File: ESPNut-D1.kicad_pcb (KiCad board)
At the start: 2 copper layers, 44 x 20 mm, 95 parts, among them J1 USB_C_Receptacle_USB2.0, J2 USB_PADS, J3 ESP_CONN, J4 ESP_CONN, J5 ESP_PROG, Q1 MMBT3904T-7-F, Q2 MMBT3904T-7-F, Q3 MMBT3906T-7-F, Q4 MMBT3906T-7-F, SW1 ESP_RST, SW2 ESP_BOOT, SW3 ESP_VDD_SW, SW4 ESPV_SEL, SW5 POW_CTRL, U1 CH340G, U2 MIC5219-3.3YM5, U3 AP22804AW5, Y1 12MHz

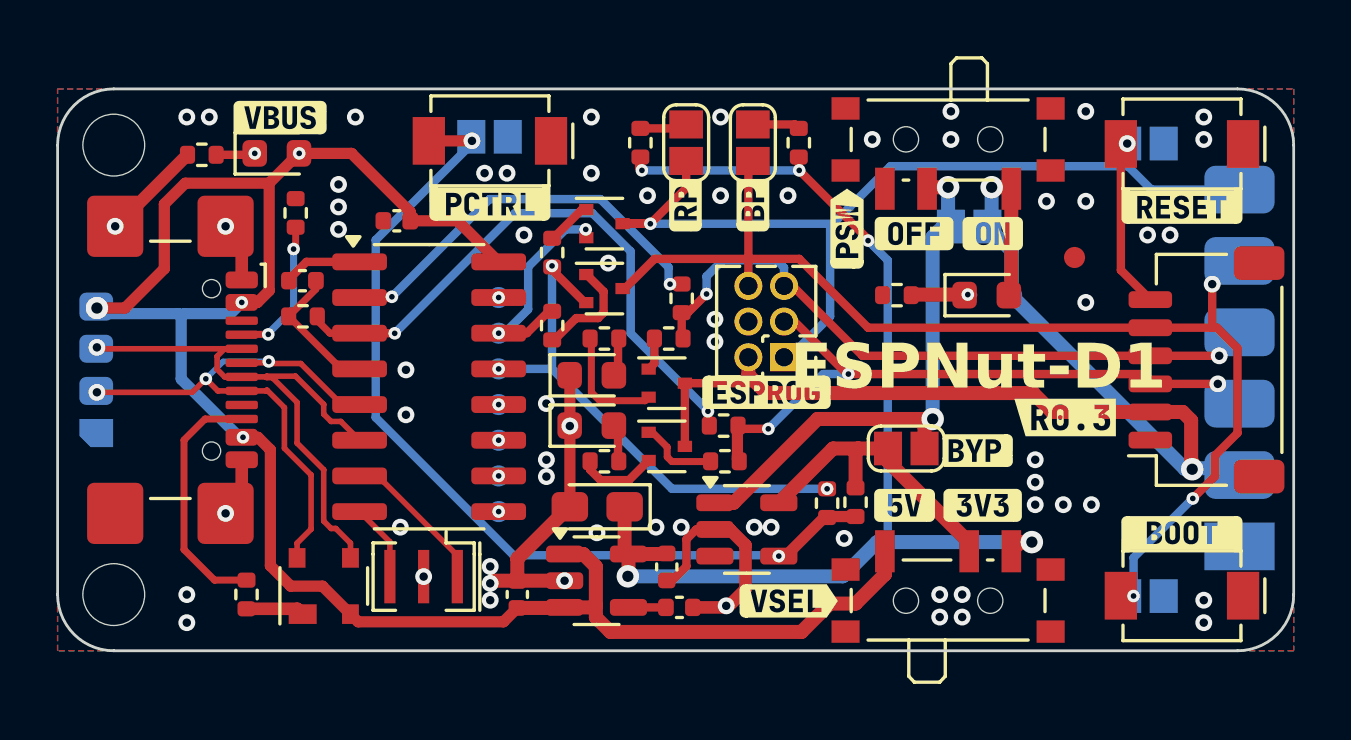
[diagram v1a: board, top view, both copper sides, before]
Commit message: Added `47 uF` 0805 capacitors
- Schematic
  - Added `47 uF` 0805 capacitors to the VBUS line, near the CH340 and `ESP_VDD_I`.
    - This was required because it was observed that the CH340 will reset when a significant load is connected to the `VBUS` line.
    - Adding two 22 uF capacitors proved to solve the issue.
    - But we are going to use 47 uF capacitors for better stability.
- PCB
  - Imported all changes to the PCB.
  - DRC passes.
- No version changes.
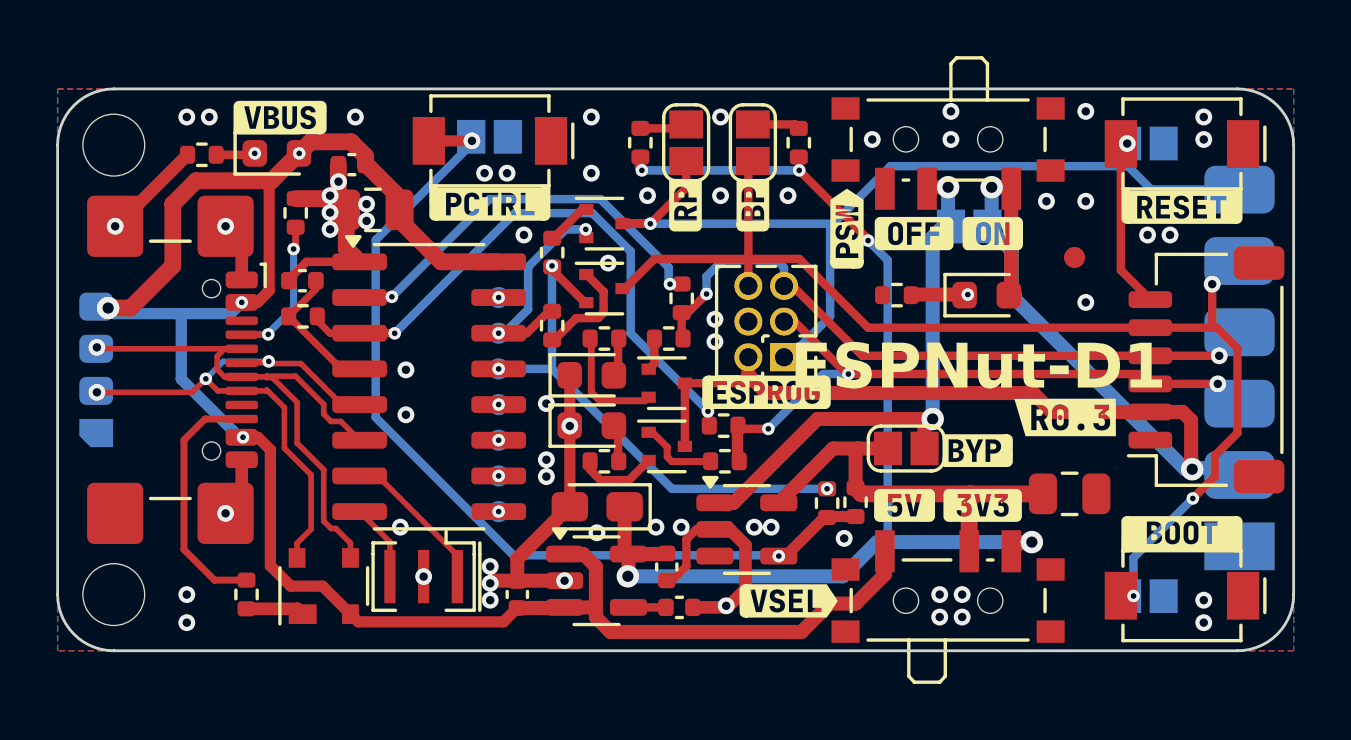
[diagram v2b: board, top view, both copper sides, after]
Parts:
- added C1: 47uF, Capacitor_SMD:C_0805_2012Metric, F.Cu at (130.2, 74.3)
- added C8: 47uF, Capacitor_SMD:C_0805_2012Metric, F.Cu at (155.0, 84.4)
- moved C3 2.56 mm to (129.5, 72.7)
- renumbered C1 to C2, C2 to C3, C3 to C4, C4 to C5, C5 to C6, C6 to C7, J3 to J2, J4 to J3, J2 to J4
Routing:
- net GND: track 31.7 -> 37.4 mm, vias 64 -> 62
- net /ESP_VDD_I: track 11.0 -> 15.0 mm

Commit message: New Revision 🆕 `R0.4`
- Schematic
  - Removed the PNP transistors from the UART activity LED circuit.
    - The SparkFun Serial Basic directly connects the LEDs to the TX and RX lines via `1K` resistors.
    - We will do the same.
    - But the voltage supplied to the LEDs can be set using a jumper `ACT-LED-V`.
  - Added jumper `TRX-PUV` to the CH340 communication lines.
    - This jumper selects between `ESP_VDD_I` and `ESP_VDD_O` for the pull-ups.
  - ERC passes.
- PCB
  - Imported all changes to the PCB.
  - Placement and routing completed.
  - DRC passes.
- This will be a test version and aesthetics don't matter now.
- Generated manufacturing files.
- New Revision 🆕 `R0.4`.
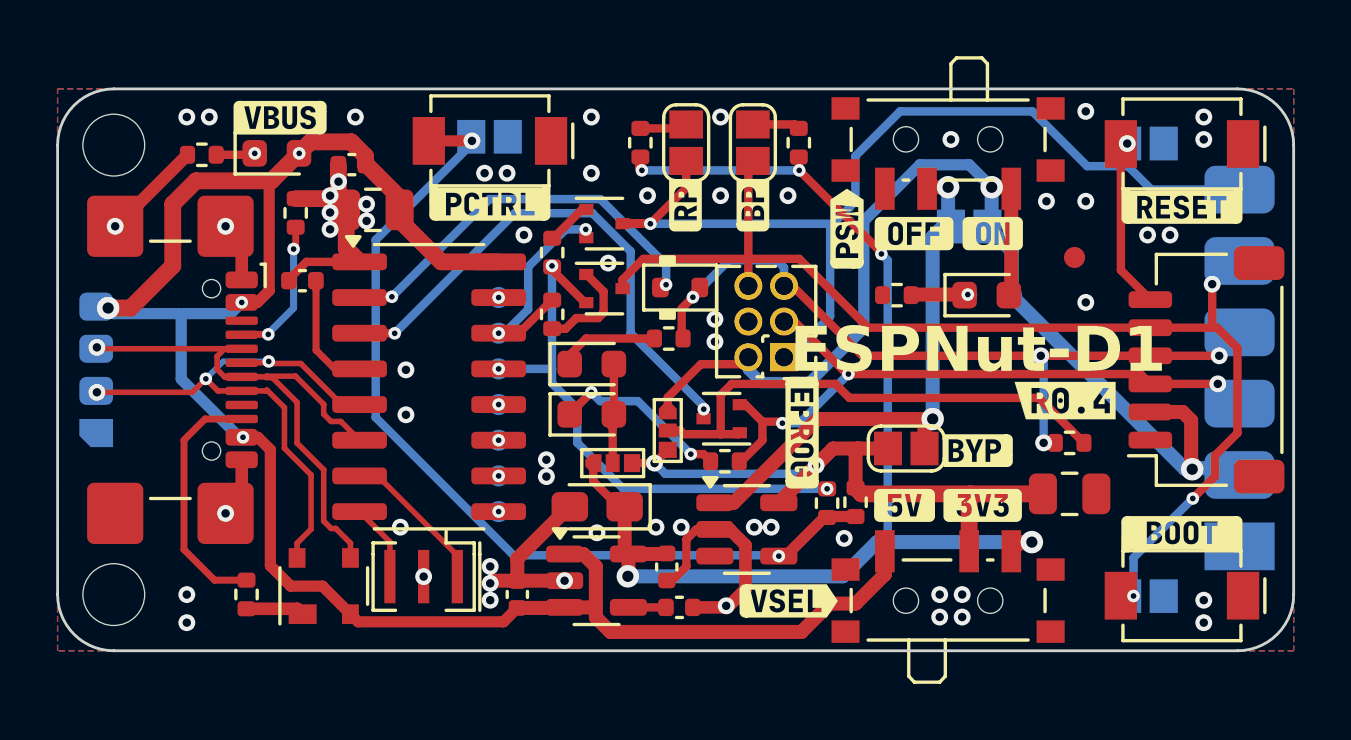
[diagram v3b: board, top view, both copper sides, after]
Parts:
- removed the Q3 at (140.7, 80.5)
- removed Q4: MMBT3906T-7-F, CSE_Package_TO_SOT_SMD:SOT-523
- removed R17, R18: 220R, Resistor_SMD:R_0402_1005Metric
- removed the R6 at (141.2, 77.5)
- removed the R8 at (142.7, 82.0)
- removed the R9 at (127.7, 78.1)
- removed kibuzzard-67F0B829: G***, kibuzzard-67F0B829
- removed kibuzzard-688DAF86: G***, kibuzzard-688DAF86
- removed kibuzzard-688DAF8E: G***, kibuzzard-688DAF8E
- added D2: BAS70K, Diode_SMD_AKL:D_SOD-523, F.Cu at (141.2, 77.1)
- added JP3: TRX-PUV, CSE_Solder-Jumper:Solder-Jumper_1x3_0402_Open, F.Cu at (140.7, 82.2)
- added JP9: ACT-LED-V, CSE_Solder-Jumper:Solder-Jumper_1x3_0402_Open, F.Cu at (138.8, 83.3)
- added Q2: 2SK3019-TP, CSE_Package_TO_SOT_SMD:SOT-523, F.Cu at (142.6, 81.7)
- added R3: 10K, Resistor_SMD:R_0402_1005Metric, F.Cu at (155.0, 82.6)
- added kibuzzard-690A4E32: G***, kibuzzard-690A4E32, F.Cu at (145.5, 82.2)
- added kibuzzard-690A4E84: G***, kibuzzard-690A4E84, F.Cu at (154.9, 81.1)
- added kibuzzard-690A4E8D: G***, kibuzzard-690A4E8D, B.Cu at (138.4, 77.2)
- moved D6 0.40 mm to (138.0, 81.6)
- moved D5 0.40 mm to (138.0, 79.8)
- moved R8 0.40 mm to (136.6, 78.0)
- renumbered D2 to D3, D3 to D4, D4 to D5, D5 to D6, JP3 to JP4, JP4 to JP5, JP5 to JP6, JP6 to JP7, JP7 to JP8, Q2 to Q3, R12 to R10, R14 to R12, R15 to R13, R16 to R14, R3 to R4, R4 to R5, R5 to R6, R10 to R8, R11 to R9
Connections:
- D5 pad 1: GND -> Net-(D5-K)
- D5 pad 2: Net-(D4-A) -> Net-(D5-A)
- D6 pad 1: GND -> Net-(D6-K)
- R13 pad 1: Net-(Q3-B) (its old number) -> Net-(D5-K)
- R14 pad 1: Net-(Q4-B) -> Net-(D6-K)
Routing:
- net Net-(JP3-C): track 0.00 -> 18.0 mm
- net /ESP_VDD_I: track 15.0 -> 22.4 mm, vias 0 -> 2
- net Net-(D6-K): track 0.00 -> 6.37 mm, vias 0 -> 2
- net GND: track 37.4 -> 32.7 mm, vias 62 -> 58
- net Net-(Q3-E): track 4.17 -> 0.00 mm
- net /CH_TX: track 23.0 -> 26.7 mm, vias 2 -> 4
- net Net-(D5-K): track 0.00 -> 3.58 mm
- net Net-(Q4-B): track 2.84 -> 0.00 mm
- net Net-(Q4-E): track 2.83 -> 0.00 mm
- net /ESP_NRST: track 40.2 -> 42.8 mm
- net Net-(D5-A): track 1.45 -> 3.99 mm
- net Net-(Q2-D): track 21.2 -> 19.0 mm
- net +3V3: track 40.9 -> 43.1 mm
- net /ESP_VDD_O: track 43.5 -> 41.9 mm
- net Net-(D4-A): track 1.39 -> 0.00 mm
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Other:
- board text added: "GND"
- board text added: "GP0"
- board text added: "NRST"
- board text added: "RX"
- board text added: "TX"
- board text added: "VO"
- board text removed: "G"
- board text removed: "N"
- board text removed: "R"
- board text removed: "T"
- board text removed: "V"

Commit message: Changed all via sizes to `0.6/0.3 mm`
- Changed all via sizes to `0.6/0.3 mm` to comply with Lion Circuits.
- Generated new manufacturing files.
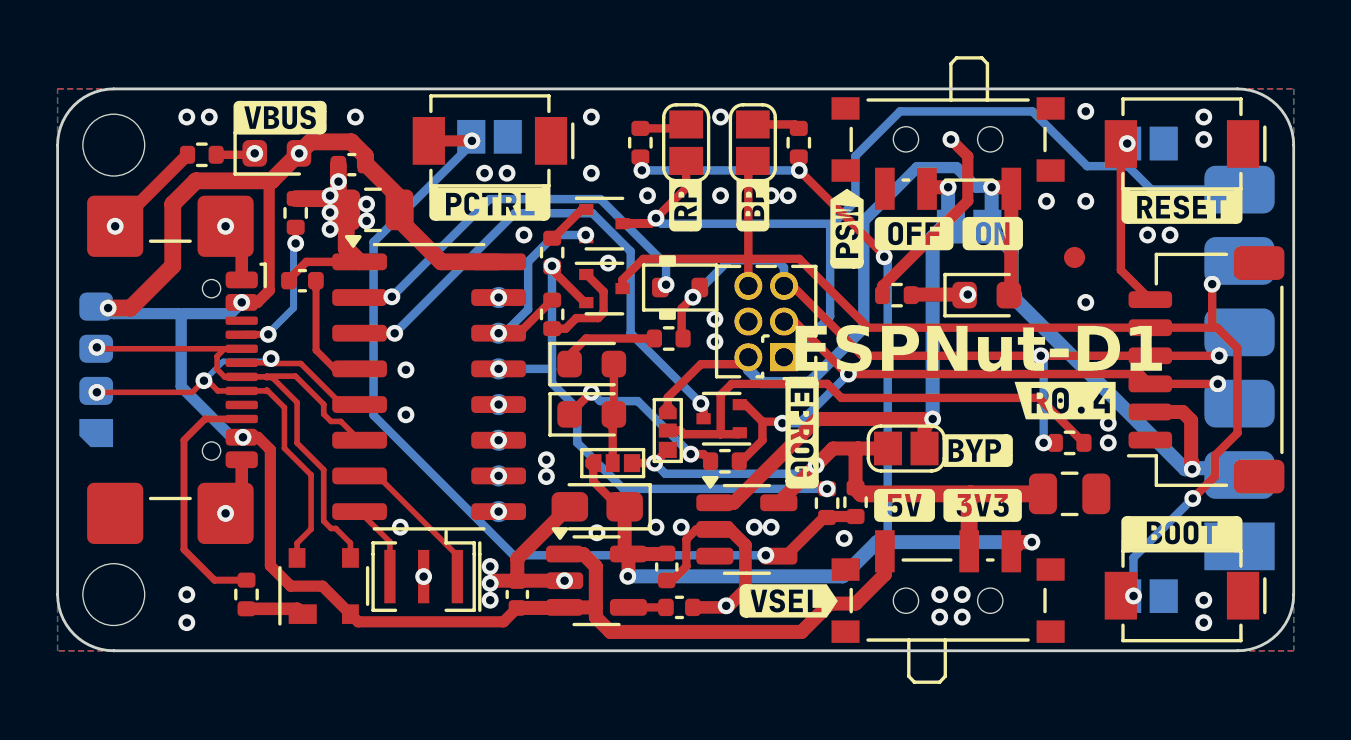
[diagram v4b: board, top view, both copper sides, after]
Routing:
- net GND: track 32.7 -> 39.8 mm, vias 58 -> 61
